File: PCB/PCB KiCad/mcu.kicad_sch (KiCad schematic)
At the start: 0 parts

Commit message: draw schematic for 60%
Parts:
- added A?: Arduino_UNO_R3, Module:Arduino_UNO_R3, symbol MCU_Module:Arduino_UNO_R3
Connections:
- new net GND: A?.29 (GND), A?.6 (GND), A?.7 (GND)
- no-connect marks 0 -> 18
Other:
- note added: "TO DO: Nets connect buttons, led"
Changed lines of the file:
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@@
 (kicad_sch (version 20211123) (generator eeschema)
   (paper "A4")
+  (junction (at 140.97 104.14) (diameter 0) (color 0 0 0 0)
+  )
+  (no_connect (at 128.27 63.5))
+  (no_connect (at 128.27 68.58))
+  (no_connect (at 128.27 71.12))
+  (no_connect (at 128.27 60.96))
+  (no_connect (at 153.67 66.04))
+  (no_connect (at 138.43 50.8))
+  (no_connect (at 153.67 96.52))
+  (no_connect (at 153.67 71.12))
+  (no_connect (at 153.67 88.9))
+  (no_connect (at 153.67 93.98))
+  (no_connect (at 153.67 76.2))
+  (no_connect (at 153.67 78.74))
+  (no_connect (at 153.67 81.28))
+  (no_connect (at 153.67 83.82))
+  (no_connect (at 153.67 86.36))
+  (no_connect (at 128.27 83.82))
+  (no_connect (at 128.27 81.28))
+  (no_connect (at 143.51 50.8))
+  (wire (pts (xy 140.97 104.14) (xy 140.97 115.57))
+    (stroke (width 0) (type default) (color 0 0 0 0))
+  )
+  (wire (pts (xy 119.38 86.36) (xy 128.27 86.36))
+    (stroke (width 0) (type default) (color 0 0 0 0))
+  )
+  (wire (pts (xy 119.38 91.44) (xy 128.27 91.44))
+    (stroke (width 0) (type default) (color 0 0 0 0))
+  )
+  (wire (pts (xy 119.38 73.66) (xy 128.27 73.66))
+    (stroke (width 0) (type default) (color 0 0 0 0))
+  )
+  (wire (pts (xy 138.43 104.14) (xy 140.97 104.14))
+    (stroke (width 0) (type default) (color 0 0 0 0))
+  )
+  (wire (pts (xy 119.38 93.98) (xy 128.27 93.98))
+    (stroke (width 0) (type default) (color 0 0 0 0))
+  )
+  (wire (pts (xy 119.38 88.9) (xy 128.27 88.9))
+    (stroke (width 0) (type default) (color 0 0 0 0))
+  )
+  (wire (pts (xy 119.38 78.74) (xy 128.27 78.74))
+    (stroke (width 0) (type default) (color 0 0 0 0))
+  )
+  (wire (pts (xy 119.38 76.2) (xy 128.27 76.2))
+    (stroke (width 0) (type default) (color 0 0 0 0))
+  )
+  (wire (pts (xy 119.38 66.04) (xy 128.27 66.04))
+    (stroke (width 0) (type default) (color 0 0 0 0))
+  )
+  (wire (pts (xy 153.67 60.96) (xy 162.56 60.96))
+    (stroke (width 0) (type default) (color 0 0 0 0))
+  )
+  (wire (pts (xy 146.05 41.91) (xy 146.05 50.8))
+    (stroke (width 0) (type default) (color 0 0 0 0))
+  )
+  (wire (pts (xy 140.97 104.14) (xy 143.51 104.14))
+    (stroke (width 0) (type default) (color 0 0 0 0))
+  )
+  (text "TO DO:\nNets\nconnect buttons, led\n" (at 34.29 38.1 0)
+    (effects (font (size 1.5 1.5)) (justify left bottom))
+  )
+  (symbol (lib_id "power:GND") (at 140.97 115.57 0) (unit 1)
+    (in_bom yes) (on_board yes) (fields_autoplaced)
+    (property "Reference" "#PWR?" (id 0) (at 140.97 121.92 0)
+      (effects (font (size 1.27 1.27)) hide)
+    )
+    (property "Value" "GND" (id 1) (at 140.97 120.65 0))
+    (property "Footprint" "" (id 2) (at 140.97 115.57 0)
+      (effects (font (size 1.27 1.27)) hide)
+    )
+    (property "Datasheet" "" (id 3) (at 140.97 115.57 0)
+      (effects (font (size 1.27 1.27)) hide)
+    )
+    (pin "1")
+  )
+  (symbol (lib_id "MCU_Module:Arduino_UNO_R3") (at 140.97 76.2 0) (unit 1)
+    (in_bom yes) (on_board yes) (fields_autoplaced)
+    (property "Reference" "A?" (id 0) (at 148.0694 48.26 0)
+      (effects (font (size 1.27 1.27)) (justify left))
+    )
+    (property "Value" "Arduino_UNO_R3" (id 1) (at 148.0694 50.8 0)
+      (effects (font (size 1.27 1.27)) (justify left))
+    )
+    (property "Footprint" "Module:Arduino_UNO_R3" (id 2) (at 140.97 76.2 0)
+      (effects (font (size 1.27 1.27) italic) hide)
+    )
+    (property "Datasheet" "https://www.arduino.cc/en/Main/arduinoBoardUno" (id 3) (at 140.97 76.2 0)
+      (effects (font (size 1.27 1.27)) hide)
+    )
+    (pin "1")
+    (pin "10")
+    (pin "11")
+    (pin "12")
+    (pin "13")
+    (pin "14")
+    (pin "15")
+    (pin "16")
+    (pin "17")
+    (pin "18")
+    (pin "19")
+    (pin "2")
+    (pin "20")
+    (pin "21")
+    (pin "22")
+    (pin "23")
+    (pin "24")
+    (pin "25")
+    (pin "26")
+    (pin "27")
+    (pin "28")
+    (pin "29")
+    (pin "3")
+    (pin "30")
+    (pin "31")
+    (pin "32")
+    (pin "4")
+    (pin "5")
+    (pin "6")
+    (pin "7")
+    (pin "8")
+    (pin "9")
+  )
 )

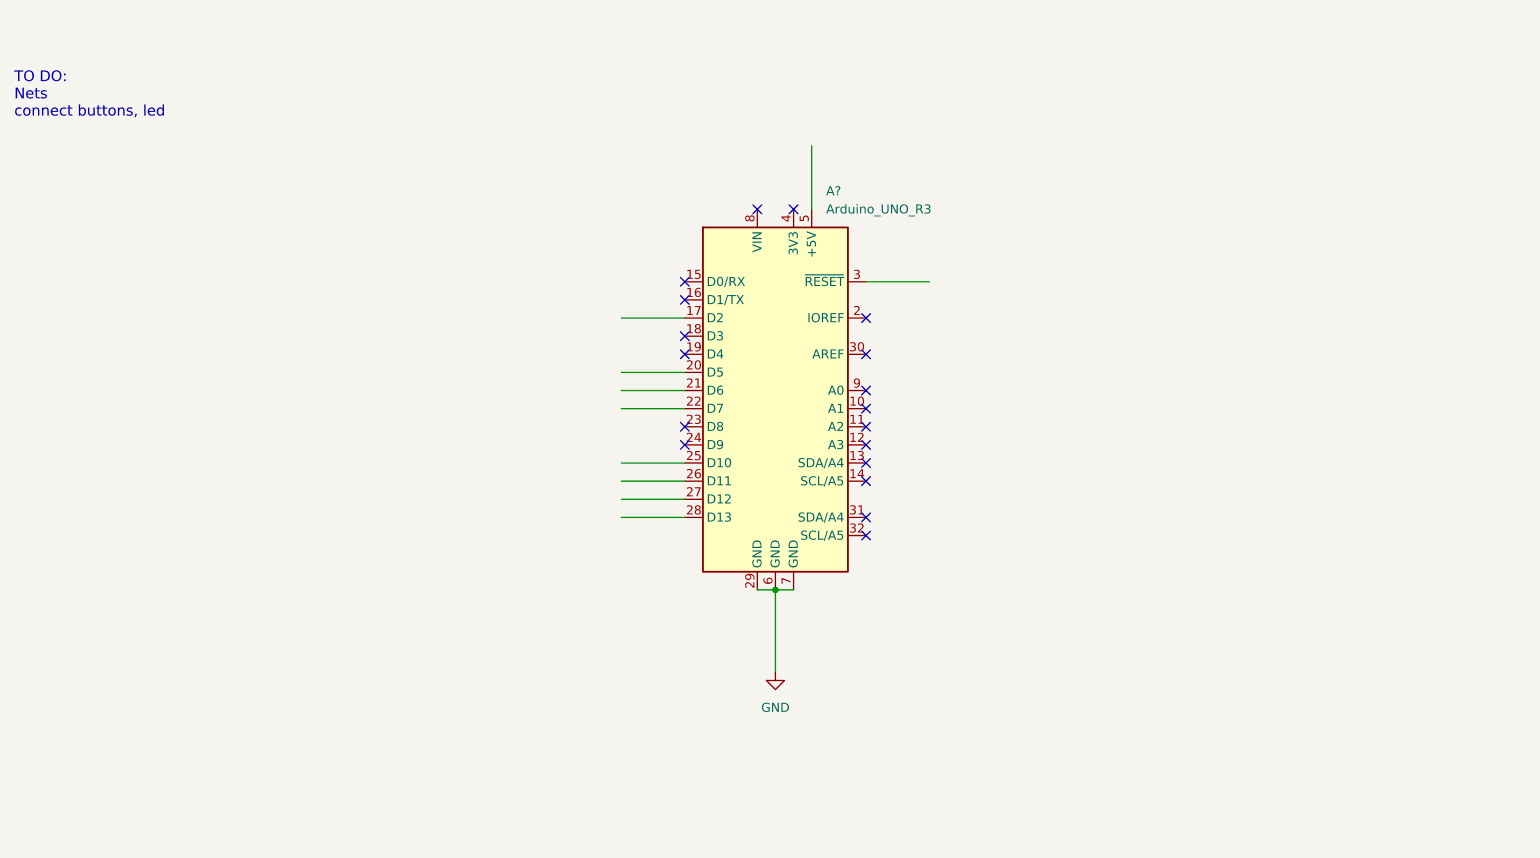
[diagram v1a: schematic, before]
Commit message: Add buttons: MCU RESET, TRIGGER
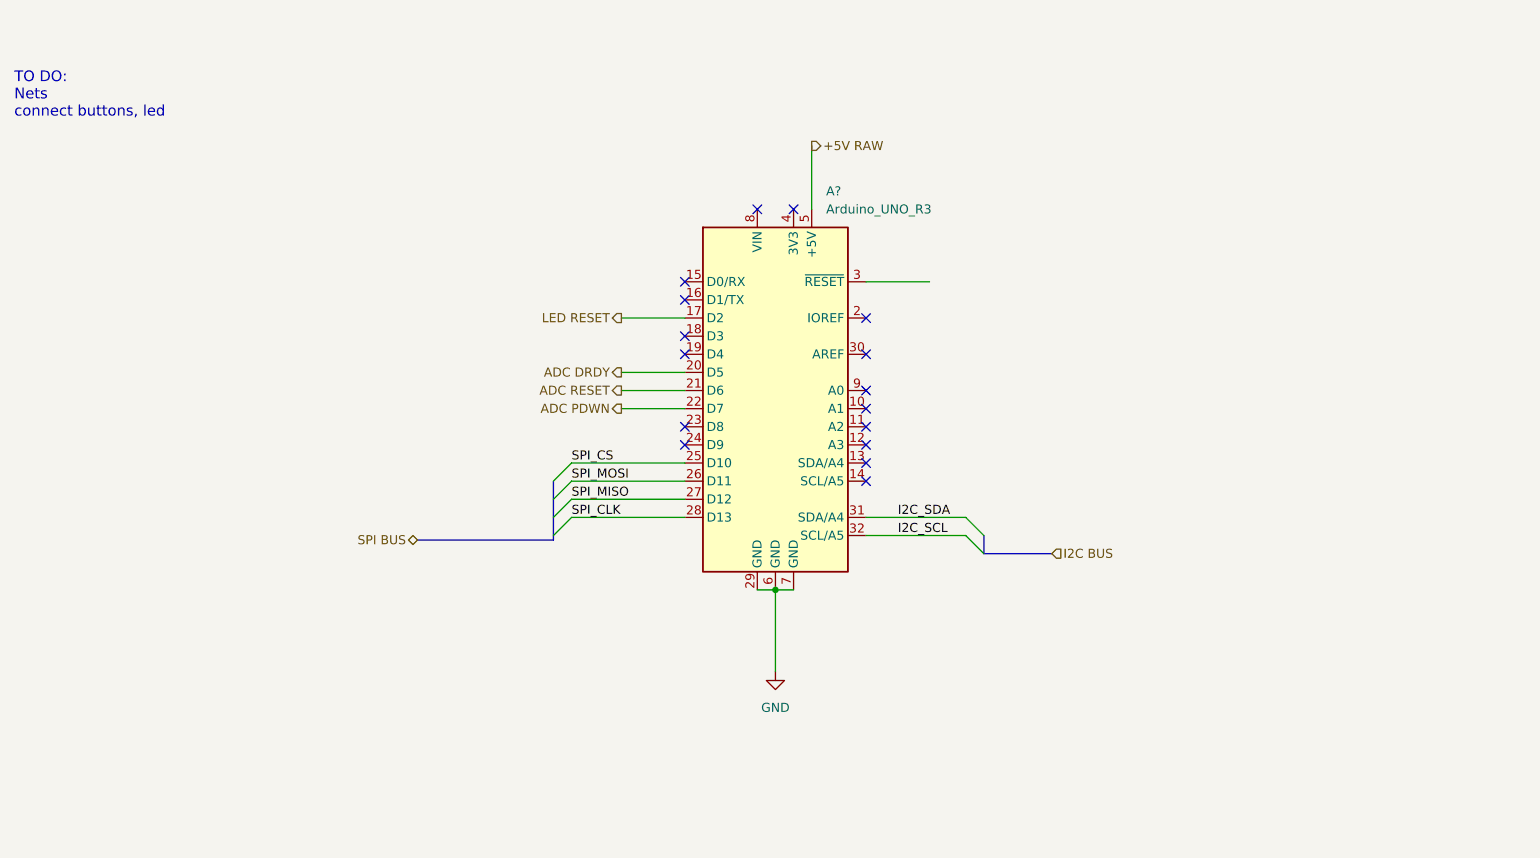
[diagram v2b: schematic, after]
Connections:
- net LED RESET: now reaches A?.17 (D2)
- net ADC DRDY: now reaches A?.20 (D5)
- net ADC RESET: now reaches A?.21 (D6)
- net ADC PDWN: now reaches A?.22 (D7)
- net SPI_CS: now reaches A?.25 (D10)
- net SPI_MOSI: now reaches A?.26 (D11)
- net SPI_MISO: now reaches A?.27 (D12)
- net SPI_CLK: now reaches A?.28 (D13)
- net I2C_SDA: now reaches A?.31 (SDA/A4)
- net I2C_SCL: now reaches A?.32 (SCL/A5)
- net +5V RAW: now reaches A?.5 (+5V)
- no-connect marks 18 -> 16
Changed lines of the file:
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@@
   (no_connect (at 153.67 66.04))
   (no_connect (at 138.43 50.8))
-  (no_connect (at 153.67 96.52))
   (no_connect (at 153.67 71.12))
   (no_connect (at 153.67 88.9))
-  (no_connect (at 153.67 93.98))
   (no_connect (at 153.67 76.2))
   (no_connect (at 153.67 78.74))
@@
   (no_connect (at 128.27 81.28))
   (no_connect (at 143.51 50.8))
+  (bus_entry (at 167.64 93.98) (size 2.54 2.54)
+    (stroke (width 0) (type default) (color 0 0 0 0))
+  )
+  (bus_entry (at 167.64 96.52) (size 2.54 2.54)
+    (stroke (width 0) (type default) (color 0 0 0 0))
+  )
+  (bus_entry (at 109.855 91.44) (size 2.54 -2.54)
+    (stroke (width 0) (type default) (color 0 0 0 0))
+  )
+  (bus_entry (at 109.855 88.9) (size 2.54 -2.54)
+    (stroke (width 0) (type default) (color 0 0 0 0))
+  )
+  (bus_entry (at 109.855 93.98) (size 2.54 -2.54)
+    (stroke (width 0) (type default) (color 0 0 0 0))
+  )
+  (bus_entry (at 109.855 96.52) (size 2.54 -2.54)
+    (stroke (width 0) (type default) (color 0 0 0 0))
+  )
   (wire (pts (xy 140.97 104.14) (xy 140.97 115.57))
     (stroke (width 0) (type default) (color 0 0 0 0))
   )
-  (wire (pts (xy 119.38 86.36) (xy 128.27 86.36))
-    (stroke (width 0) (type default) (color 0 0 0 0))
-  )
-  (wire (pts (xy 119.38 91.44) (xy 128.27 91.44))
+  (bus (pts (xy 90.805 97.155) (xy 109.855 97.155))
     (stroke (width 0) (type default) (color 0 0 0 0))
   )
@@
     (stroke (width 0) (type default) (color 0 0 0 0))
   )
-  (wire (pts (xy 119.38 93.98) (xy 128.27 93.98))
+  (wire (pts (xy 112.395 86.36) (xy 128.27 86.36))
     (stroke (width 0) (type default) (color 0 0 0 0))
   )
-  (wire (pts (xy 119.38 88.9) (xy 128.27 88.9))
+  (wire (pts (xy 153.67 93.98) (xy 167.64 93.98))
+    (stroke (width 0) (type default) (color 0 0 0 0))
+  )
+  (bus (pts (xy 109.855 96.52) (xy 109.855 97.155))
+    (stroke (width 0) (type default) (color 0 0 0 0))
+  )
+  (bus (pts (xy 109.855 91.44) (xy 109.855 93.98))
+    (stroke (width 0) (type default) (color 0 0 0 0))
+  )
+  (bus (pts (xy 170.18 96.52) (xy 170.18 99.06))
     (stroke (width 0) (type default) (color 0 0 0 0))
   )
@@
     (stroke (width 0) (type default) (color 0 0 0 0))
   )
+  (bus (pts (xy 170.18 99.06) (xy 179.705 99.06))
+    (stroke (width 0) (type default) (color 0 0 0 0))
+  )
   (wire (pts (xy 119.38 76.2) (xy 128.27 76.2))
+    (stroke (width 0) (type default) (color 0 0 0 0))
+  )
+  (wire (pts (xy 112.395 93.98) (xy 128.27 93.98))
+    (stroke (width 0) (type default) (color 0 0 0 0))
+  )
+  (wire (pts (xy 153.67 96.52) (xy 167.64 96.52))
+    (stroke (width 0) (type default) (color 0 0 0 0))
+  )
+  (wire (pts (xy 112.395 88.9) (xy 128.27 88.9))
+    (stroke (width 0) (type default) (color 0 0 0 0))
+  )
+  (bus (pts (xy 109.855 93.98) (xy 109.855 96.52))
     (stroke (width 0) (type default) (color 0 0 0 0))
   )
@@
     (stroke (width 0) (type default) (color 0 0 0 0))
   )
+  (wire (pts (xy 112.395 91.44) (xy 128.27 91.44))
+    (stroke (width 0) (type default) (color 0 0 0 0))
+  )
   (wire (pts (xy 140.97 104.14) (xy 143.51 104.14))
+    (stroke (width 0) (type default) (color 0 0 0 0))
+  )
+  (bus (pts (xy 109.855 88.9) (xy 109.855 91.44))
     (stroke (width 0) (type default) (color 0 0 0 0))
   )
@@
     (effects (font (size 1.5 1.5)) (justify left bottom))
   )
+  (label "SPI_MISO" (at 112.395 91.44 0)
+    (effects (font (size 1.27 1.27)) (justify left bottom))
+  )
+  (label "I2C_SCL" (at 158.115 96.52 0)
+    (effects (font (size 1.27 1.27)) (justify left bottom))
+  )
+  (label "SPI_CLK" (at 112.395 93.98 0)
+    (effects (font (size 1.27 1.27)) (justify left bottom))
+  )
+  (label "SPI_CS" (at 112.395 86.36 0)
+    (effects (font (size 1.27 1.27)) (justify left bottom))
+  )
+  (label "SPI_MOSI" (at 112.395 88.9 0)
+    (effects (font (size 1.27 1.27)) (justify left bottom))
+  )
+  (label "I2C_SDA" (at 158.115 93.98 0)
+    (effects (font (size 1.27 1.27)) (justify left bottom))
+  )
+  (hierarchical_label "ADC RESET" (shape output) (at 119.38 76.2 180)
+    (effects (font (size 1.27 1.27)) (justify right))
+  )
+  (hierarchical_label "SPI BUS" (shape bidirectional) (at 90.805 97.155 180)
+    (effects (font (size 1.27 1.27)) (justify right))
+  )
+  (hierarchical_label "ADC PDWN" (shape output) (at 119.38 78.74 180)
+    (effects (font (size 1.27 1.27)) (justify right))
+  )
+  (hierarchical_label "I2C BUS" (shape input) (at 179.705 99.06 0)
+    (effects (font (size 1.27 1.27)) (justify left))
+  )
+  (hierarchical_label "LED RESET" (shape output) (at 119.38 66.04 180)
+    (effects (font (size 1.27 1.27)) (justify right))
+  )
+  (hierarchical_label "+5V RAW" (shape output) (at 146.05 41.91 0)
+    (effects (font (size 1.27 1.27)) (justify left))
+  )
+  (hierarchical_label "ADC DRDY" (shape output) (at 119.38 73.66 180)
+    (effects (font (size 1.27 1.27)) (justify right))
+  )
   (symbol (lib_id "power:GND") (at 140.97 115.57 0) (unit 1)

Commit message: Merge MCU and IO into single sheet, wire LEDs
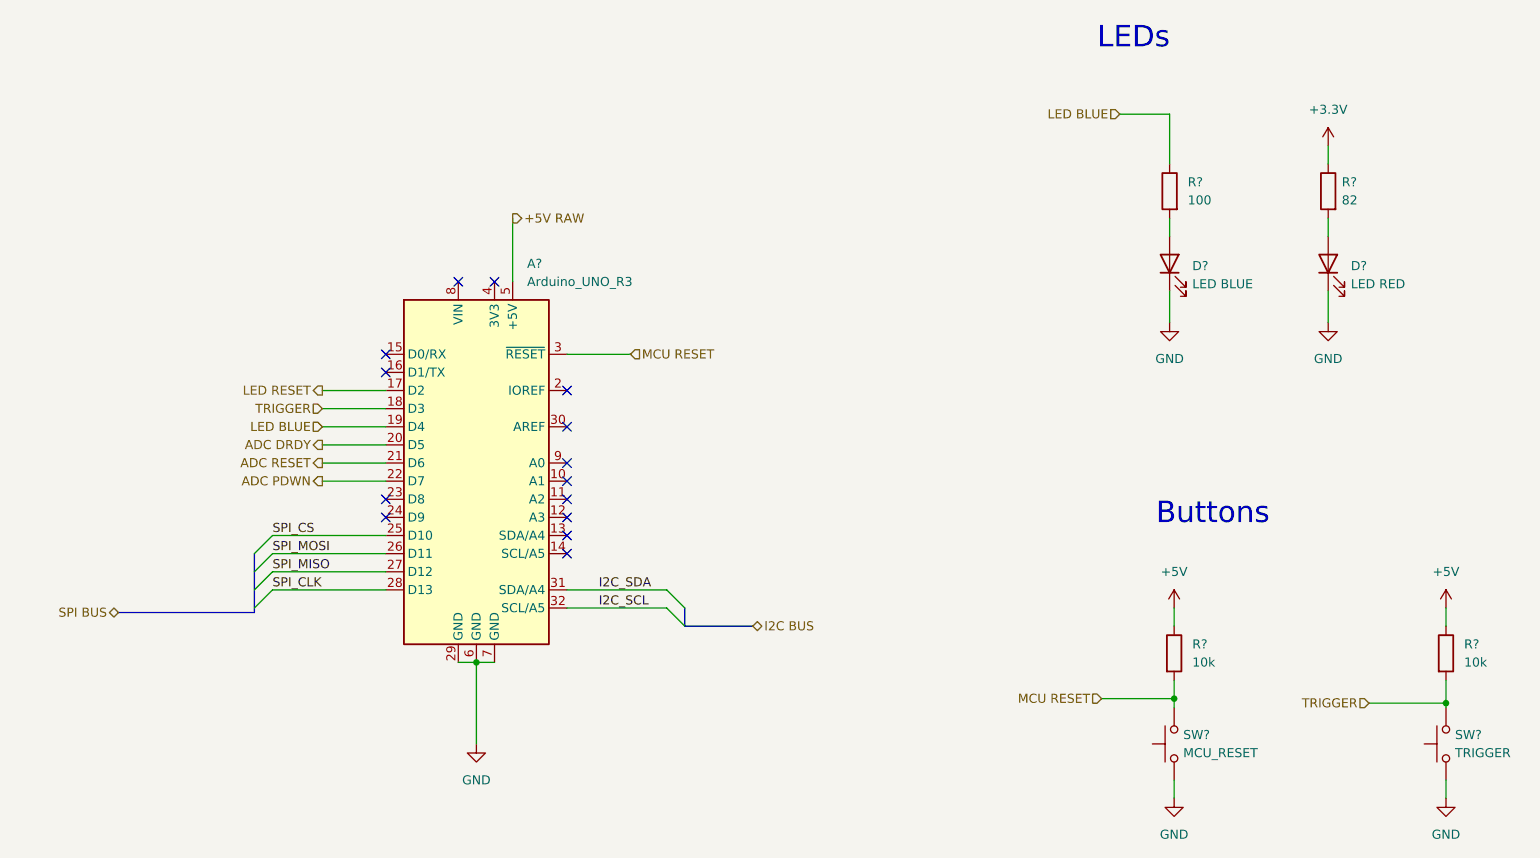
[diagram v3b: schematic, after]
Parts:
- added D?: LED RED, symbol Device:LED
- added D?: LED BLUE, symbol Device:LED
- added R? (x2): 10k, symbol Device:R
- added R?: 100, symbol Device:R
- added R?: 82, symbol Device:R
- added SW?: MCU_RESET, symbol Switch:SW_Push
- added SW?: TRIGGER, symbol Switch:SW_Push
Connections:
- net GND: now also D?.1 (K), D?.1 (K), SW?.1, SW?.1
- net TRIGGER: now reaches A?.18 (D3)
- net TRIGGER: now also R?.2, SW?.2
- net LED BLUE: now reaches A?.19 (D4)
- net LED BLUE: now also R?.1
- net MCU RESET: now reaches A?.3 (~{RESET})
- net MCU RESET: now also R?.2, SW?.2
- new net: D?.2 (A), R?.2 (x2)
- new net +3V3: R?.1
- new net +5V: R?.1, R?.1
- no-connect marks 16 -> 14
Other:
- note added: "Buttons"
- note added: "LEDs"
- note removed: "TO DO: Nets connect buttons, led"
- moved on the sheet: A?
